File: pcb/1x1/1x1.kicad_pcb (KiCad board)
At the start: 2 copper layers, 16 x 16 mm, 9 parts, among them J1 Conn_02x04_Odd_Even

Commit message: 1x1 pcb updated
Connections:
- J1 pad 1: Net-(J1-Pin_1) -> unconnected-(J1-Pin_1-Pad1)
- J1 pad 2: Net-(J1-Pin_2) -> unconnected-(J1-Pin_2-Pad2)
- J1 pad 3: Net-(J1-Pin_3) -> unconnected-(J1-Pin_3-Pad3)
- J1 pad 4: Net-(J1-Pin_4) -> unconnected-(J1-Pin_4-Pad4)
- J1 pad 5: Net-(J1-Pin_5) -> unconnected-(J1-Pin_5-Pad5)
- J1 pad 6: Net-(J1-Pin_6) -> unconnected-(J1-Pin_6-Pad6)
- J1 pad 7: Net-(J1-Pin_7) -> unconnected-(J1-Pin_7-Pad7)
- J1 pad 8: Net-(J1-Pin_8) -> unconnected-(J1-Pin_8-Pad8)
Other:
- outline, holes or cut-outs redrawn
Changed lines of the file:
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@@
   (net 7 "Net-(J1-Pin_6)")
   (net 8 "Net-(J1-Pin_8)")
+  (net 9 "unconnected-(J1-Pin_1-Pad1)")
+  (net 10 "unconnected-(J1-Pin_2-Pad2)")
+  (net 11 "unconnected-(J1-Pin_3-Pad3)")
+  (net 12 "unconnected-(J1-Pin_4-Pad4)")
+  (net 13 "unconnected-(J1-Pin_5-Pad5)")
+  (net 14 "unconnected-(J1-Pin_6-Pad6)")
+  (net 15 "unconnected-(J1-Pin_7-Pad7)")
+  (net 16 "unconnected-(J1-Pin_8-Pad8)")
   (footprint "Connector_PinSocket_2.54mm:PinSocket_2x04_P2.54mm_Vertical" (layer "F.Cu")
     (at 4.2 6.71 90)
@@
       (stroke (width 0.1) (type solid)) (layer "F.Fab"))
     (pad "1" thru_hole rect (at 0 0 90) (size 1.7 1.7) (drill 1) (layers "*.Cu" "*.Mask")
-      (net 1 "Net-(J1-Pin_1)") (pinfunction "Pin_1") (pintype "passive"))
+      (net 9 "unconnected-(J1-Pin_1-Pad1)") (pinfunction "Pin_1") (pintype "passive"))
     (pad "2" thru_hole oval (at -2.54 0 90) (size 1.7 1.7) (drill 1) (layers "*.Cu" "*.Mask")
-      (net 5 "Net-(J1-Pin_2)") (pinfunction "Pin_2") (pintype "passive"))
+      (net 10 "unconnected-(J1-Pin_2-Pad2)") (pinfunction "Pin_2") (pintype "passive"))
     (pad "3" thru_hole oval (at 0 2.54 90) (size 1.7 1.7) (drill 1) (layers "*.Cu" "*.Mask")
-      (net 2 "Net-(J1-Pin_3)") (pinfunction "Pin_3") (pintype "passive"))
+      (net 11 "unconnected-(J1-Pin_3-Pad3)") (pinfunction "Pin_3") (pintype "passive"))
     (pad "4" thru_hole oval (at -2.54 2.54 90) (size 1.7 1.7) (drill 1) (layers "*.Cu" "*.Mask")
-      (net 6 "Net-(J1-Pin_4)") (pinfunction "Pin_4") (pintype "passive"))
+      (net 12 "unconnected-(J1-Pin_4-Pad4)") (pinfunction "Pin_4") (pintype "passive"))
     (pad "5" thru_hole oval (at 0 5.08 90) (size 1.7 1.7) (drill 1) (layers "*.Cu" "*.Mask")
-      (net 3 "Net-(J1-Pin_5)") (pinfunction "Pin_5") (pintype "passive"))
+      (net 13 "unconnected-(J1-Pin_5-Pad5)") (pinfunction "Pin_5") (pintype "passive"))
     (pad "6" thru_hole oval (at -2.54 5.08 90) (size 1.7 1.7) (drill 1) (layers "*.Cu" "*.Mask")
-      (net 7 "Net-(J1-Pin_6)") (pinfunction "Pin_6") (pintype "passive"))
+      (net 14 "unconnected-(J1-Pin_6-Pad6)") (pinfunction "Pin_6") (pintype "passive"))
     (pad "7" thru_hole oval (at 0 7.62 90) (size 1.7 1.7) (drill 1) (layers "*.Cu" "*.Mask")
-      (net 4 "Net-(J1-Pin_7)") (pinfunction "Pin_7") (pintype "passive"))
+      (net 15 "unconnected-(J1-Pin_7-Pad7)") (pinfunction "Pin_7") (pintype "passive"))
     (pad "8" thru_hole oval (at -2.54 7.62 90) (size 1.7 1.7) (drill 1) (layers "*.Cu" "*.Mask")
-      (net 8 "Net-(J1-Pin_8)") (pinfunction "Pin_8") (pintype "passive"))
+      (net 16 "unconnected-(J1-Pin_8-Pad8)") (pinfunction "Pin_8") (pintype "passive"))
     (model "${KICAD6_3DMODEL_DIR}/Connector_PinSocket_2.54mm.3dshapes/PinSocket_2x04_P2.54mm_Vertical.wrl"
       (offset (xyz 0 0 0))
@@
       (net 5 "Net-(J1-Pin_2)") (pinfunction "1") (pintype "input"))
   )
-  (gr_line (start 0 0) (end 16 0)
-    (stroke (width 0.1) (type default)) (layer "Edge.Cuts"))
-  (gr_arc (start 0 6) (mid 2 8) (end 0 10)
-    (stroke (width 0.1) (type default)) (layer "Edge.Cuts"))
-  (gr_line (start 16 6) (end 16 0)
-    (stroke (width 0.1) (type default)) (layer "Edge.Cuts"))
-  (gr_line (start 0 10) (end 0 16)
-    (stroke (width 0.1) (type default)) (layer "Edge.Cuts"))
-  (gr_line (start 0 16) (end 16 16)
-    (stroke (width 0.1) (type default)) (layer "Edge.Cuts"))
-  (gr_line (start 0 0) (end 0 6)
-    (stroke (width 0.1) (type default)) (layer "Edge.Cuts"))
-  (gr_arc (start 16 10) (mid 14 8) (end 16 6)
-    (stroke (width 0.1) (type default)) (layer "Edge.Cuts"))
-  (gr_line (start 16 16) (end 16 10)
-    (stroke (width 0.1) (type default)) (layer "Edge.Cuts"))
+  (gr_rect (start 0 0) (end 16 16)
+    (stroke (width 0.1) (type default)) (fill none) (layer "Edge.Cuts"))
 )

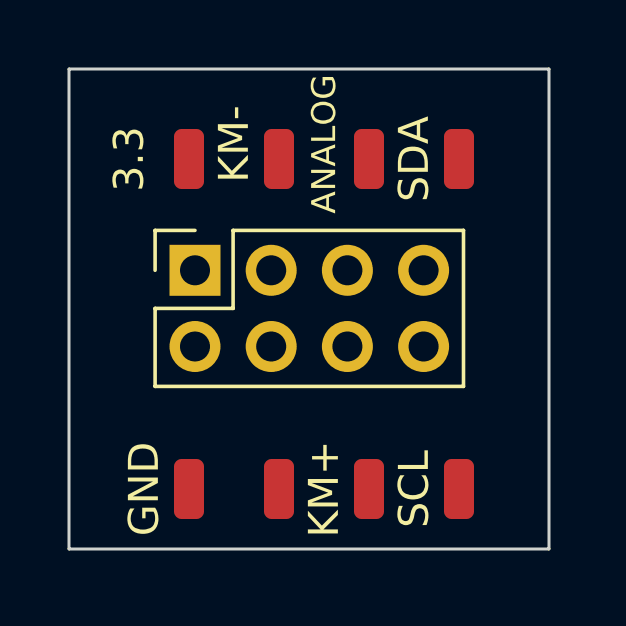
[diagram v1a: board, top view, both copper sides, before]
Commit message: kicad version 8.0, 1x1 pcb
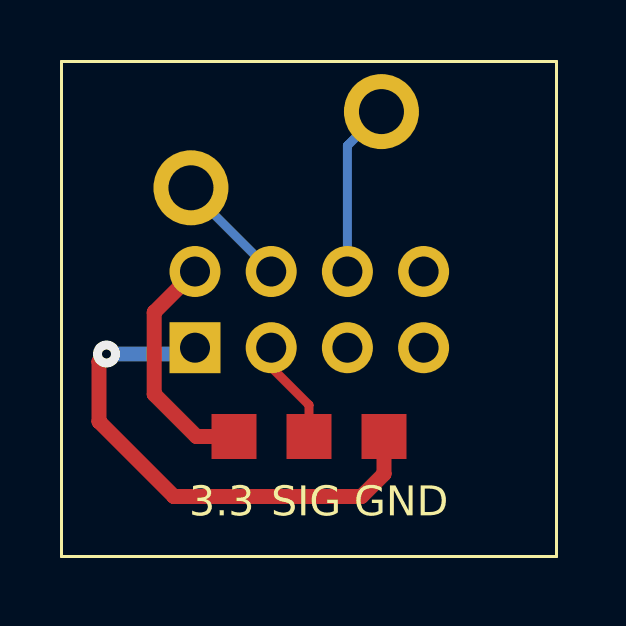
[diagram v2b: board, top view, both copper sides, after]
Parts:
- removed 3.3, ANALOG, GND, H7, KM+, KM-, SCL, SDA: MountingHole_Pad, Connector_Wire:SolderWirePad_1x01_SMD_1x2mm
- added SW1: SW_Push, PCM_Switch_Keyboard_Cherry_MX:SW_Cherry_MX_Plate, F.Cu at (7.88, 6.50)
- added TP1: TestPoint, TestPoint:TestPoint_Pad_1.5x1.5mm, F.Cu at (8.00, 12.2)
- added TP2: TestPoint, TestPoint:TestPoint_Pad_1.5x1.5mm, F.Cu at (10.5, 12.2)
- added TP3: TestPoint, TestPoint:TestPoint_Pad_1.5x1.5mm, F.Cu at (5.50, 12.2)
- J1: moved to B.Cu
- moved J1 2.58 mm to (4.20, 9.29), turned to -90 degrees
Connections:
- J1 pad 1: unconnected-(J1-Pin_1-Pad1) -> Net-(J1-Pin_1)
- J1 pad 2: unconnected-(J1-Pin_2-Pad2) -> Net-(J1-Pin_2)
- J1 pad 3: unconnected-(J1-Pin_3-Pad3) -> Net-(J1-Pin_3)
- J1 pad 4: unconnected-(J1-Pin_4-Pad4) -> Net-(J1-Pin_4)
- J1 pad 6: unconnected-(J1-Pin_6-Pad6) -> Net-(J1-Pin_6)
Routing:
- net Net-(J1-Pin_1): track 0.00 -> 17.5 mm, vias 0 -> 1
- net Net-(J1-Pin_2): track 0.00 -> 7.90 mm
- net Net-(J1-Pin_6): track 0.00 -> 5.80 mm
- net Net-(J1-Pin_4): track 0.00 -> 3.90 mm
- net Net-(J1-Pin_3): track 0.00 -> 3.48 mm
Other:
- board outline removed
- board text added: "3.3"
- board text added: "GND"
- board text added: "SIG"

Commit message: pcb 1x1 sync
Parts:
- moved J1 0.35 mm to (4.45, 9.54)
- moved SW1 0.35 mm to (8.12, 6.75)
- moved TP1 0.35 mm to (8.25, 12.5)
- moved TP2 0.35 mm to (10.8, 12.5)
- moved TP3 0.35 mm to (5.75, 12.5)
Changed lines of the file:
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@@
 	(footprint "TestPoint:TestPoint_Pad_1.5x1.5mm"
 		(layer "F.Cu")
-		(at 10.5 12.25)
+		(at 10.75 12.5)
 		(descr "SMD rectangular pad as test Point, square 1.5mm side length")
 		(tags "test point SMD pad rectangle square")
@@
 	(footprint "TestPoint:TestPoint_Pad_1.5x1.5mm"
 		(layer "F.Cu")
-		(at 5.5 12.25)
+		(at 5.75 12.5)
 		(descr "SMD rectangular pad as test Point, square 1.5mm side length")
 		(tags "test point SMD pad rectangle square")
@@
 	(footprint "TestPoint:TestPoint_Pad_1.5x1.5mm"
 		(layer "F.Cu")
-		(at 8 12.25)
+		(at 8.25 12.5)
 		(descr "SMD rectangular pad as test Point, square 1.5mm side length")
 		(tags "test point SMD pad rectangle square")
@@
 	(footprint "PCM_Switch_Keyboard_Cherry_MX:SW_Cherry_MX_Plate"
 		(layer "F.Cu")
-		(at 7.875 6.5)
+		(at 8.125 6.75)
 		(descr "Cherry MX keyswitch Plate Mount")
 		(tags "Cherry MX Keyboard Keyswitch Switch Plate Cutout")
@@
 	)
 	(footprint "Connector_PinSocket_2.54mm:PinSocket_2x04_P2.54mm_Vertical"
-		(locked yes)
 		(layer "B.Cu")
-		(at 4.2 9.29 -90)
+		(at 4.45 9.54 -90)
 		(descr "Through hole straight socket strip, 2x04, 2.54mm pitch, double cols (from Kicad 4.0.7), script generated")
 		(tags "Through hole socket strip THT 2x04 2.54mm double row")
@@
 	)
 	(gr_rect
-		(start -0.25 -0.25)
-		(end 16.25 16.25)
-		(locked yes)
+		(start 0 0)
+		(end 16.5 16.5)
 		(stroke
 			(width 0.1)
@@
 		(layer "F.SilkS")
 	)
-	(gr_rect
-		(start 4.25 15.5)
-		(end 11.75 17.5)
-		(stroke
-			(width 0.15)
-			(type default)
-		)
-		(fill none)
-		(layer "Dwgs.User")
-	)
-	(gr_line
-		(start 10.5 12.5)
-		(end 10.5 15.5)
-		(stroke
-			(width 0.8)
-			(type default)
-		)
-		(layer "Dwgs.User")
-	)
-	(gr_line
-		(start 5.5 12.5)
-		(end 5.5 15.5)
-		(stroke
-			(width 0.8)
-			(type default)
-		)
-		(layer "Dwgs.User")
-	)
-	(gr_line
-		(start 8 12.5)
-		(end 8 15.5)
-		(stroke
-			(width 0.8)
-			(type default)
-		)
-		(layer "Dwgs.User")
-	)
 	(gr_text "3.3"
-		(at 4 15 0)
+		(at 4.25 15.25 0)
 		(layer "F.SilkS")
 		(effects
@@
 	)
 	(gr_text "SIG"
-		(at 6.735715 15 0)
+		(at 6.985715 15.25 0)
 		(layer "F.SilkS")
 		(effects
@@
 	)
 	(gr_text "GND"
-		(at 9.5 15 0)
+		(at 9.75 15.25 0)
 		(layer "F.SilkS")
 		(effects
@@
 	)
 	(segment
-		(start 6.74 6.75)
-		(end 4.065 4.075)
+		(start 6.99 7)
+		(end 4.315 4.325)
 		(width 0.3)
 		(layer "B.Cu")
@@
 	)
 	(segment
-		(start 4.065 4.075)
-		(end 4.065 3.96)
+		(start 4.315 4.325)
+		(end 4.315 4.21)
 		(width 0.3)
 		(layer "B.Cu")
@@
 	)
 	(segment
-		(start 9.28 6.75)
-		(end 9.28 2.555)
+		(start 9.53 7)
+		(end 9.53 2.805)
 		(width 0.3)
 		(layer "B.Cu")
@@
 	)
 	(segment
-		(start 9.28 2.555)
-		(end 10.415 1.42)
+		(start 9.53 2.805)
+		(end 10.665 1.67)
 		(width 0.3)
 		(layer "B.Cu")
@@
 	)
 	(segment
-		(start 8 11.2)
-		(end 6.74 9.94)
+		(start 8.25 11.45)
+		(end 6.99 10.19)
 		(width 0.3)
 		(layer "F.Cu")
@@
 	)
 	(segment
-		(start 6.74 9.94)
-		(end 6.74 9.29)
+		(start 6.99 10.19)
+		(end 6.99 9.54)
 		(width 0.3)
 		(layer "F.Cu")
@@
 	)
 	(segment
-		(start 8 12.25)
-		(end 8 11.2)
+		(start 8.25 12.5)
+		(end 8.25 11.45)
 		(width 0.3)
 		(layer "F.Cu")
@@
 	)
 	(segment
-		(start 9.75 14.25)
-		(end 3.5 14.25)
+		(start 10 14.5)
+		(end 3.75 14.5)
 		(width 0.5)
 		(layer "F.Cu")
@@
 	)
 	(segment
-		(start 10.5 12.25)
-		(end 10.5 13.5)
+		(start 10.75 12.5)
+		(end 10.75 13.75)
 		(width 0.5)
 		(layer "F.Cu")
@@
 	)
 	(segment
-		(start 10.5 13.5)
-		(end 9.75 14.25)
+		(start 10.75 13.75)
+		(end 10 14.5)
 		(width 0.5)
 		(layer "F.Cu")
@@
 	)
 	(segment
-		(start 1 9.75)
-		(end 1.25 9.5)
+		(start 1.25 10)
+		(end 1.5 9.75)
 		(width 0.5)
 		(layer "F.Cu")
@@
 	)
 	(segment
-		(start 3.5 14.25)
-		(end 1 11.75)
+		(start 3.75 14.5)
+		(end 1.25 12)
 		(width 0.5)
 		(layer "F.Cu")
@@
 	)
 	(segment
-		(start 1 11.75)
-		(end 1 9.75)
+		(start 1.25 12)
+		(end 1.25 10)
 		(width 0.5)
 		(layer "F.Cu")
@@
 	)
 	(via
-		(at 1.25 9.5)
+		(at 1.5 9.75)
 		(size 0.9)
 		(drill 0.3)
@@
 	)
 	(segment
-		(start 1.25 9.5)
-		(end 3.99 9.5)
+		(start 1.5 9.75)
+		(end 4.24 9.75)
 		(width 0.5)
 		(layer "B.Cu")
@@
 	)
 	(segment
-		(start 3.99 9.5)
-		(end 4.2 9.29)
+		(start 4.24 9.75)
+		(end 4.45 9.54)
 		(width 0.5)
 		(layer "B.Cu")
@@
 	)
 	(segment
-		(start 5.5 12.25)
-		(end 4.25 12.25)
+		(start 5.75 12.5)
+		(end 4.5 12.5)
 		(width 0.5)
 		(layer "F.Cu")
@@
 	)
 	(segment
-		(start 2.84 10.84)
-		(end 2.84 8.11)
+		(start 3.09 11.09)
+		(end 3.09 8.36)
 		(width 0.5)
 		(layer "F.Cu")
@@
 	)
 	(segment
-		(start 4.25 12.25)
-		(end 2.84 10.84)
+		(start 4.5 12.5)
+		(end 3.09 11.09)
 		(width 0.5)
 		(layer "F.Cu")
@@
 	)
 	(segment
-		(start 2.84 8.11)
-		(end 4.2 6.75)
+		(start 3.09 8.36)
+		(end 4.45 7)
 		(width 0.5)
 		(layer "F.Cu")
 		(net 8)
 	)
+	(group ""
+		(members "0c135175-a099-48ac-aeba-853512bca50d" "22e562be-d6c2-4592-8d6b-d5240938552e"
+			"230cbc67-778c-4747-98ef-4b8a575b3398" "2b83875f-453e-44f2-9988-29eec695e375"
+			"3b1defd3-6595-473b-afde-936d988cae9c" "3bd26f5c-1151-4bca-8395-a38191cb26ae"
+			"4be51fed-9d2f-488c-bb78-5551fc454827" "538e550a-a875-44da-b286-aef072ebb876"
+			"65673f39-d3a2-4c85-aec4-16f97a4185f6" "66eb1448-f2e7-4207-b76b-20a3aaae2fc6"
+			"6a1d5882-8d63-4011-80a3-e4a25d5b9969" "72727f99-f366-4272-9d34-113b196e64d7"
+			"8898c26a-8a30-43f4-9542-f7835620852d" "a29d0cfb-4d49-41a3-bbb5-6166698eda8e"
+			"a6ebf16b-ec2c-482c-a5b5-78447953d043" "b1e3ab74-68b0-4c02-9135-86217cdf91d2"
+			"b33b61e3-8756-4f59-a425-10eec9bb35d7" "b5839378-041c-43a3-aa09-18a0f17fbd7f"
+			"c671fe42-9d5e-4d41-b245-7dbfd924746c" "c93ff858-25ec-495a-9ee4-a07c55a42d0f"
+			"cee5d891-e317-4017-8582-2736ff02497e" "cf40a6c9-04c6-4921-ae18-34d4edf9ce7d"
+			"d40d1ecf-1d2c-4e51-a97f-919b4ccaaf98" "d98f1aac-ff58-4e9f-9ef8-f28ab99bf7cb"
+			"dbd6544a-9e52-4290-abd9-5e3f4f779e36" "dc11ac07-0243-4b52-9fcc-7a6ec4d11fe6"
+			"e2d1d1e6-76f8-423a-a01d-994193155227" "eaaa80f7-0dd7-49d8-9fa1-d3dd4181ccf6"
+			"fd66a5b7-c19c-4e5f-8396-97fd9fefa0bb"
+		)
+	)
 )
